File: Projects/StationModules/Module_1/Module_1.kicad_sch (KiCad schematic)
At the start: 55 parts, among them M1 BluePillStm32, U1 PC817, U2 L7805, U3 TC1047AxNB, U5 LM311, U6 6N137

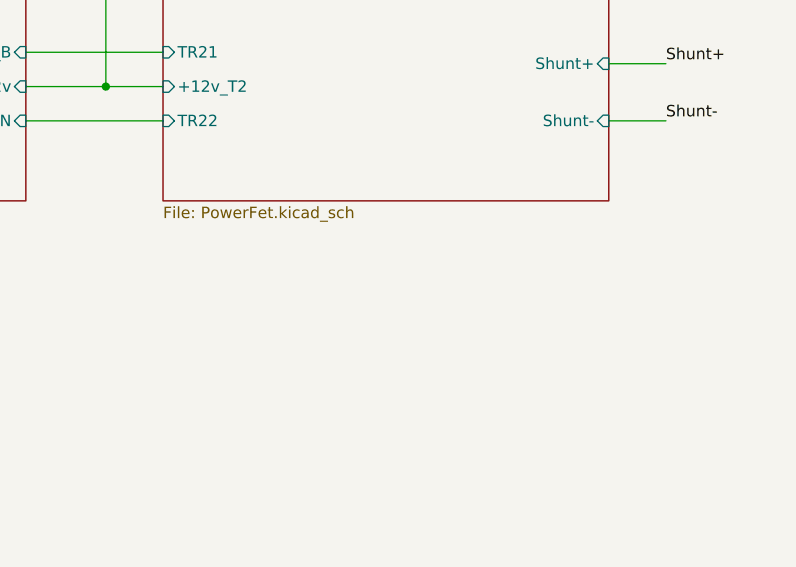
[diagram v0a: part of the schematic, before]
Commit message: Place elements 1
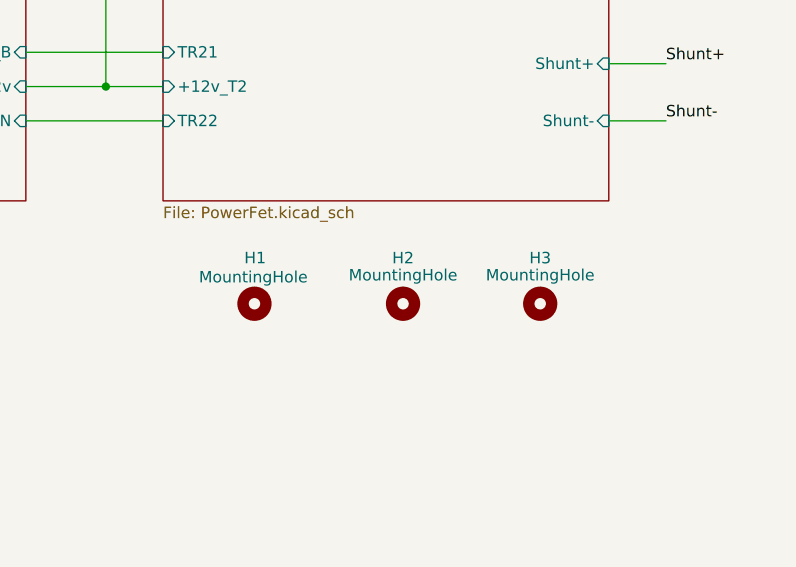
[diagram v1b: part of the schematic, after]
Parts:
- added H1, H2, H3: MountingHole, MountingHole:MountingHole_3.5mm, symbol Mechanical:MountingHole
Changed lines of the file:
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@@
+    )
+  )
+  (symbol (lib_id "Mechanical:MountingHole") (at 238.76 146.05 0) (unit 1)
+    (in_bom yes) (on_board yes) (dnp no)
+    (property "Reference" "H2" (at 238.76 140.97 0)
+      (effects (font (size 1.27 1.27)))
+    )
+    (property "Value" "MountingHole" (at 238.76 142.875 0)
+      (effects (font (size 1.27 1.27)))
+    )
+    (property "Footprint" "MountingHole:MountingHole_3.5mm" (at 238.76 146.05 0)
+      (effects (font (size 1.27 1.27)) hide)
+    )
+    (property "Datasheet" "~" (at 238.76 146.05 0)
+      (effects (font (size 1.27 1.27)) hide)
+    )
+    (instances
+      (project "Module_1"
+        (path "/52aeb9ce-9f3b-4d8f-8c36-7e23df4a5f32"
+          (reference "H2") (unit 1)
+        )
+      )
     )
   )
@@
     )
   )
+  (symbol (lib_id "Mechanical:MountingHole") (at 222.25 146.05 0) (unit 1)
+    (in_bom yes) (on_board yes) (dnp no)
+    (property "Reference" "H1" (at 221.1158 140.9618 0)
+      (effects (font (size 1.27 1.27)) (justify left))
+    )
+    (property "Value" "MountingHole" (at 216.0801 143.0922 0)
+      (effects (font (size 1.27 1.27)) (justify left))
+    )
+    (property "Footprint" "MountingHole:MountingHole_3.5mm" (at 222.25 146.05 0)
+      (effects (font (size 1.27 1.27)) hide)
+    )
+    (property "Datasheet" "~" (at 222.25 146.05 0)
+      (effects (font (size 1.27 1.27)) hide)
+    )
+    (instances
+      (project "Module_1"
+        (path "/52aeb9ce-9f3b-4d8f-8c36-7e23df4a5f32"
+          (reference "H1") (unit 1)
+        )
+      )
+    )
+  )
   (symbol (lib_id "Device:C_Small") (at 53.34 113.03 0) (unit 1)
     (in_bom yes) (on_board yes) (dnp no) (fields_autoplaced)
@@
         )
       )
+    )
+  )
+  (symbol (lib_id "Mechanical:MountingHole") (at 254 146.05 0) (unit 1)
+    (in_bom yes) (on_board yes) (dnp no)
+    (property "Reference" "H3" (at 254 140.97 0)
+      (effects (font (size 1.27 1.27)))
+    )
+    (property "Value" "MountingHole" (at 254 142.875 0)
+      (effects (font (size 1.27 1.27)))
+    )
+    (property "Footprint" "MountingHole:MountingHole_3.5mm" (at 254 146.05 0)
+      (effects (font (size 1.27 1.27)) hide)
+    )
+    (property "Datasheet" "~" (at 254 146.05 0)
+      (effects (font (size 1.27 1.27)) hide)
+    )
+    (instances
+      (project "Module_1"
+        (path "/52aeb9ce-9f3b-4d8f-8c36-7e23df4a5f32"
+          (reference "H3") (unit 1)
+        )
+      )

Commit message: Trace complit 1
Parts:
- added C29: 0,1uF, Capacitor_SMD:C_1206_3216Metric, symbol Device:C_Small
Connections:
- net +3.3V is gone; now on net +3V3: C1.1, M1.20 (3V3)
- net +5V: now also C29.1
- net GND: now also C29.2
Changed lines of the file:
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@@
   (junction (at 132.08 57.15) (diameter 0) (color 0 0 0 0)
   )
+  (junction (at 101.6 104.14) (diameter 0) (color 0 0 0 0)
+  )
   (junction (at 34.29 90.17) (diameter 0) (color 0 0 0 0)
   )
   (junction (at 59.69 137.16) (diameter 0) (color 0 0 0 0)
   )
+  (junction (at 22.86 80.01) (diameter 0) (color 0 0 0 0)
+  )
   (junction (at 52.07 137.16) (diameter 0) (color 0 0 0 0)
   )
@@
   )
   (junction (at 152.4 48.26) (diameter 0) (color 0 0 0 0)
-  )
-  (junction (at 22.86 80.01) (diameter 0) (color 0 0 0 0)
   )
   (junction (at 218.44 62.23) (diameter 0) (color 0 0 0 0)
@@
     (stroke (width 0) (type default))
   )
+  (wire (pts (xy 78.74 104.14) (xy 101.6 104.14))
+    (stroke (width 0) (type default))
+  )
   (wire (pts (xy 44.45 110.49) (xy 53.34 110.49))
     (stroke (width 0) (type default))
@@
     (stroke (width 0) (type default))
   )
+  (wire (pts (xy 78.74 110.49) (xy 78.74 120.65))
+    (stroke (width 0) (type default))
+  )
   (wire (pts (xy 152.4 22.86) (xy 152.4 25.4))
     (stroke (width 0) (type default))
@@
     (stroke (width 0) (type default))
   )
+  (wire (pts (xy 78.74 105.41) (xy 78.74 104.14))
+    (stroke (width 0) (type default))
+  )
   (wire (pts (xy 218.44 48.26) (xy 214.63 48.26))
     (stroke (width 0) (type default))
@@
   )
   (wire (pts (xy 101.6 78.74) (xy 105.41 78.74))
+    (stroke (width 0) (type default))
+  )
+  (wire (pts (xy 78.74 120.65) (xy 101.6 120.65))
     (stroke (width 0) (type default))
   )
@@
     )
   )
-  (symbol (lib_id "power:+3.3V") (at 22.86 80.01 0) (unit 1)
-    (in_bom yes) (on_board yes) (dnp no) (fields_autoplaced)
-    (property "Reference" "#PWR01" (at 22.86 83.82 0)
-      (effects (font (size 1.27 1.27)) hide)
-    )
-    (property "Value" "+3.3V" (at 22.86 76.2 0)
-      (effects (font (size 1.27 1.27)))
-    )
-    (property "Footprint" "" (at 22.86 80.01 0)
-      (effects (font (size 1.27 1.27)) hide)
-    )
-    (property "Datasheet" "" (at 22.86 80.01 0)
-      (effects (font (size 1.27 1.27)) hide)
-    )
-    (pin "1")
-    (instances
-      (project "Module_1"
-        (path "/52aeb9ce-9f3b-4d8f-8c36-7e23df4a5f32"
-          (reference "#PWR01") (unit 1)
-        )
-      )
-    )
-  )
   (symbol (lib_id "Z_led:Led") (at 118.11 71.12 0) (unit 1)
     (in_bom yes) (on_board yes) (dnp no)
@@
         (path "/52aeb9ce-9f3b-4d8f-8c36-7e23df4a5f32"
           (reference "R18") (unit 1)
+        )
+      )
+    )
+  )
+  (symbol (lib_id "Device:C_Small") (at 78.74 107.95 0) (unit 1)
+    (in_bom yes) (on_board yes) (dnp no) (fields_autoplaced)
+    (property "Reference" "C29" (at 81.28 107.3213 0)
+      (effects (font (size 1.27 1.27)) (justify left))
+    )
+    (property "Value" "0,1uF" (at 81.28 109.8613 0)
+      (effects (font (size 1.27 1.27)) (justify left))
+    )
+    (property "Footprint" "Capacitor_SMD:C_1206_3216Metric" (at 78.74 107.95 0)
+      (effects (font (size 1.27 1.27)) hide)
+    )
+    (property "Datasheet" "~" (at 78.74 107.95 0)
+      (effects (font (size 1.27 1.27)) hide)
+    )
+    (property "ID" "" (at 78.74 107.95 0)
+      (effects (font (size 1.27 1.27)) hide)
+    )
+    (pin "1")
+    (pin "2")
+    (instances
+      (project "Module_1"
+        (path "/52aeb9ce-9f3b-4d8f-8c36-7e23df4a5f32"
+          (reference "C29") (unit 1)
         )
       )
@@
         )
       )
+    )
+  )
+  (symbol (lib_id "power:+3V3") (at 22.86 80.01 0) (unit 1)
+    (in_bom yes) (on_board yes) (dnp no) (fields_autoplaced)
+    (property "Reference" "#PWR028" (at 22.86 83.82 0)
+      (effects (font (size 1.27 1.27)) hide)
+    )
+    (property "Value" "+3V3" (at 22.86 76.2 0)
+      (effects (font (size 1.27 1.27)))
+    )
+    (property "Footprint" "" (at 22.86 80.01 0)
+      (effects (font (size 1.27 1.27)) hide)
+    )
+    (property "Datasheet" "" (at 22.86 80.01 0)
+      (effects (font (size 1.27 1.27)) hide)
+    )
+    (pin "1")
+    (instances
+      (project "Module_1"
+        (path "/52aeb9ce-9f3b-4d8f-8c36-7e23df4a5f32"
+          (reference "#PWR028") (unit 1)
+        )
+      )

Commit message: Trace complit 2
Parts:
- U5: footprint Package_SO:SO-8_5.3x6.2mm_P1.27mm -> Package_SO:SO-8_3.9x4.9mm_P1.27mm
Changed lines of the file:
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@@
       (effects (font (size 1.27 1.27)))
     )
-    (property "Footprint" "Package_SO:SO-8_5.3x6.2mm_P1.27mm" (at 240.03 53.34 0)
+    (property "Footprint" "Package_SO:SO-8_3.9x4.9mm_P1.27mm" (at 240.03 53.34 0)
       (effects (font (size 1.27 1.27)) hide)
     )

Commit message: add bom module 1
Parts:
- added C30: 0,1uF, Capacitor_SMD:C_1206_3216Metric, symbol Device:C_Small
- C1, C11, C12, C16, C18, C2, C29, C5, C7, C8: LCSC (none) -> C82601; MFR.Part (none) -> CC1206KRX7R9BB104
- C10, C9: LCSC (none) -> C469628; MFR.Part (none) -> CC1206JRNPOBBN100
- C13, C14, C15: LCSC (none) -> C274377; MFR.Part (none) -> CC1206KRX7R9BB334
- C17: LCSC (none) -> C527247; MFR.Part (none) -> CC1206GRNPO9BN102
- C3, C6: LCSC (none) -> C88730; MFR.Part (none) -> 25PX470MEFC8X11.5
- C4: footprint Capacitor_Tantalum_SMD:CP_EIA-6032-28_Kemet-C -> Capacitor_Tantalum_SMD:CP_EIA-7343-15_Kemet-W; ID T495C107K016ATE200 -> (none); LCSC (none) -> C122302; MFR.Part (none) -> T491D107K020AT
- D1, D5, D6: LCSC (none) -> C2891733; MFR.Part (none) -> LL4148
- D2: LCSC (none) -> C3013853; MFR.Part (none) -> TLHR5400
- D3: LCSC (none) -> C5334366; MFR.Part (none) -> TLHY4405
- D4, D7: LCSC (none) -> C3001646; MFR.Part (none) -> TLHG4400
- J1: LCSC (none) -> C5665; MFR.Part (none) -> C5665
- JP1, JP2: LCSC (none) -> C6332196; MFR.Part (none) -> HB-PH3-25413PB2GOP
- R1, R11, R15, R9: LCSC (none) -> C136458; MFR.Part (none) -> RC1206JR-074K7L
- R10: LCSC (none) -> C137199; MFR.Part (none) -> RC1206JR-0715KL
- R12: LCSC (none) -> C137124; MFR.Part (none) -> RC1206JR-07680RL
- R13, R5, R6, R7: LCSC (none) -> C137152; MFR.Part (none) -> RC1206JR-07330RL
- R14, R18: LCSC (none) -> C137189; MFR.Part (none) -> RC1206JR-071K5L
- R16: LCSC (none) -> C246069; MFR.Part (none) -> RC1206JR-07360RL
- R17: LCSC (none) -> C112223; MFR.Part (none) -> RC1206JR-071KL
- R2: LCSC (none) -> C114948; MFR.Part (none) -> RC1206JR-07470RL
- R3, R4: value 4k7 -> 4,7k; LCSC (none) -> C136458; MFR.Part (none) -> RC1206JR-074K7L
- R8: LCSC (none) -> C113307; MFR.Part (none) -> RC1206JR-07100RL
- RV1, RV2: value 4k7 3296W -> 5k; LCSC (none) -> C118907; MFR.Part (none) -> 3296W-1-502
- U1: LCSC (none) -> C2833074; MFR.Part (none) -> PC817X2YSZW
- U2: LCSC (none) -> C2935188; MFR.Part (none) -> L7805ABP
- U3: LCSC (none) -> C50052; MFR.Part (none) -> TC1047AVNBTR
- U4: value ~ -> 78L05S; LCSC (none) -> C2858514; MFR.Part (none) -> 78L05S
- U5: LCSC (none) -> C2868397; MFR.Part (none) -> LM311PSR
- U6: LCSC (none) -> C142297; MFR.Part (none) -> 6N137
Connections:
- net GND: now also C30.2
- net OS: now also C30.1

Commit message: finaly on summer
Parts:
- D2: LCSC C3013853 -> C99771
- D3: LCSC C5334366 -> C85160
- D4, D7: LCSC C3001646 -> C2895476
- JP1, JP2: LCSC C6332196 -> C49257
- R17: LCSC C112223 -> C4410; MFR.Part RC1206JR-071KL -> 1206W4F1001T5E
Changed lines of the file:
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@@
       (effects (font (size 1.27 1.27)) hide)
     )
-    (property "LCSC" "C3013853" (at 118.11 64.77 0)
+    (property "LCSC" "C99771" (at 118.11 64.77 0)
       (effects (font (size 1.27 1.27)) hide)
     )
@@
       (effects (font (size 1.27 1.27)) hide)
     )
-    (property "LCSC" "C3001646" (at 179.07 48.26 0)
+    (property "LCSC" "C2895476" (at 179.07 48.26 0)
       (effects (font (size 1.27 1.27)) hide)
     )
@@
       (effects (font (size 1.27 1.27)) hide)
     )
-    (property "LCSC" "C6332196" (at 130.81 181.61 0)
+    (property "LCSC" "C49257" (at 130.81 181.61 0)
       (effects (font (size 1.27 1.27)) hide)
     )
@@
       (effects (font (size 1.27 1.27)) hide)
     )
-    (property "LCSC" "C5334366" (at 118.11 71.12 0)
+    (property "LCSC" "C85160" (at 118.11 71.12 0)
       (effects (font (size 1.27 1.27)) hide)
     )
@@
       (effects (font (size 1.27 1.27)) hide)
     )
-    (property "MFR.Part" "RC1206JR-071KL" (at 227.33 27.94 0)
-      (effects (font (size 1.27 1.27)) hide)
-    )
-    (property "Description" "250mW Thick Film Resistors ±100ppm/℃ ±5% 1kΩ 1206 Chip Resistor - Surface Mount ROHS" (at 227.33 27.94 0)
-      (effects (font (size 1.27 1.27)) hide)
-    )
-    (property "LCSC" "C112223" (at 227.33 27.94 0)
+    (property "MFR.Part" "1206W4F1001T5E" (at 227.33 27.94 0)
+      (effects (font (size 1.27 1.27)) hide)
+    )
+    (property "Description" "250mW Thick Film Resistors ±1% 1kΩ 1206 Chip Resistor - Surface Mount ROHS" (at 227.33 27.94 0)
+      (effects (font (size 1.27 1.27)) hide)
+    )
+    (property "LCSC" "C4410" (at 227.33 27.94 0)
       (effects (font (size 1.27 1.27)) hide)
     )
@@
       (effects (font (size 1.27 1.27)) hide)
     )
-    (property "LCSC" "C6332196" (at 130.81 165.1 0)
+    (property "LCSC" "C49257" (at 130.81 165.1 0)
       (effects (font (size 1.27 1.27)) hide)
     )
@@
       (effects (font (size 1.27 1.27)) hide)
     )
-    (property "LCSC" "C3001646" (at 118.11 78.74 0)
-      (effects (font (size 1.27 1.27)) hide)
-    )
+    (property "LCSC" "C2895476" (at 118.11 78.74 0)
+      (effects (font (size 1.27 1.27)) hide)
+    )

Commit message: change module1,2
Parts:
- C10, C9: value 10pF -> 10nF; LCSC C469628 -> C9194; MFR.Part CC1206JRNPOBBN100 -> 1206B103K102NT
- R16: value 360 -> 150; LCSC C246069 -> C25353; MFR.Part RC1206JR-07360RL -> 1206W4J0151T5E
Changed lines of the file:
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@@
       (effects (font (size 1.27 1.27)) (justify right))
     )
-    (property "Value" "360" (at 220.98 57.785 0)
+    (property "Value" "150" (at 220.98 57.785 0)
       (effects (font (size 1.27 1.27)) (justify right))
     )
@@
       (effects (font (size 1.27 1.27)) hide)
     )
-    (property "MFR.Part" "RC1206JR-07360RL" (at 218.44 55.88 0)
-      (effects (font (size 1.27 1.27)) hide)
-    )
-    (property "Description" "250mW Thick Film Resistors ±100ppm/℃ ±5% 360Ω 1206 Chip Resistor - Surface Mount ROHS" (at 218.44 55.88 0)
-      (effects (font (size 1.27 1.27)) hide)
-    )
-    (property "LCSC" "C246069" (at 218.44 55.88 0)
+    (property "MFR.Part" "1206W4J0151T5E" (at 218.44 55.88 0)
+      (effects (font (size 1.27 1.27)) hide)
+    )
+    (property "Description" "250mW Thick Film Resistors ±100ppm/℃ ±5% 150Ω 1206 Chip Resistor - Surface Mount ROHS" (at 218.44 55.88 0)
+      (effects (font (size 1.27 1.27)) hide)
+    )
+    (property "LCSC" "C25353" (at 218.44 55.88 0)
       (effects (font (size 1.27 1.27)) hide)
     )
@@
       (effects (font (size 1.27 1.27)) (justify left))
     )
-    (property "Value" "10pF" (at 123.19 142.8813 0)
+    (property "Value" "10nF" (at 123.19 142.8813 0)
       (effects (font (size 1.27 1.27)) (justify left))
     )
@@
       (effects (font (size 1.27 1.27)) hide)
     )
-    (property "MFR.Part" "CC1206JRNPOBBN100" (at 120.65 140.97 0)
-      (effects (font (size 1.27 1.27)) hide)
-    )
-    (property "Description" "500V 10pF NP0 ±5% 1206 Multilayer Ceramic Capacitors MLCC - SMD/SMT ROHS" (at 120.65 140.97 0)
-      (effects (font (size 1.27 1.27)) hide)
-    )
-    (property "LCSC" "C469628" (at 120.65 140.97 0)
+    (property "MFR.Part" "1206B103K102NT" (at 120.65 140.97 0)
+      (effects (font (size 1.27 1.27)) hide)
+    )
+    (property "Description" "1kV 10nF X7R ±10% 1206 Multilayer Ceramic Capacitors MLCC - SMD/SMT ROHS" (at 120.65 140.97 0)
+      (effects (font (size 1.27 1.27)) hide)
+    )
+    (property "LCSC" "C9194" (at 120.65 140.97 0)
       (effects (font (size 1.27 1.27)) hide)
     )
@@
       (effects (font (size 1.27 1.27)) (justify left))
     )
-    (property "Value" "10pF" (at 114.3 178.4413 0)
+    (property "Value" "10nF" (at 114.3 178.4413 0)
       (effects (font (size 1.27 1.27)) (justify left))
     )
@@
       (effects (font (size 1.27 1.27)) hide)
     )
-    (property "MFR.Part" "CC1206JRNPOBBN100" (at 111.76 176.53 0)
-      (effects (font (size 1.27 1.27)) hide)
-    )
-    (property "Description" "500V 10pF NP0 ±5% 1206 Multilayer Ceramic Capacitors MLCC - SMD/SMT ROHS" (at 111.76 176.53 0)
-      (effects (font (size 1.27 1.27)) hide)
-    )
-    (property "LCSC" "C469628" (at 111.76 176.53 0)
-      (effects (font (size 1.27 1.27)) hide)
-    )
+    (property "MFR.Part" "1206B103K102NT" (at 111.76 176.53 0)
+      (effects (font (size 1.27 1.27)) hide)
+    )
+    (property "Description" "1kV 10nF X7R ±10% 1206 Multilayer Ceramic Capacitors MLCC - SMD/SMT ROHS" (at 111.76 176.53 0)
+      (effects (font (size 1.27 1.27)) hide)
+    )
+    (property "LCSC" "C9194" (at 111.76 176.53 0)
+      (effects (font (size 1.27 1.27)) hide)
+    )

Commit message: change on 25_02_24
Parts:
- C1, C10, C11, C12, C13, C14, C15, C16, C17, C18, C2, C29, C3, C30, C4, C5, C6, C7, C8, C9, D1, D2, D3, D4, D5, D6, D7, J1, JP1, JP2, R1, R10, R11, R13, R14, R15, R16, R17, R18, R3, R4, R5, R6, R7, R8, R9, RV1, RV2, U1, U3, U4, U5, U6: Mounting (none) -> Yes
- H1, H2, H3, M1: Mounting (none) -> No
- R12: LCSC C137124 -> C25392; MFR.Part RC1206JR-07680RL -> 1206W4J0681T5E; Mounting (none) -> Yes
- R2: LCSC C114948 -> C114945; MFR.Part RC1206JR-07470RL -> RC1206FR-07470RL; Mounting (none) -> Yes
- U2: LCSC C2935188 -> C3795; MFR.Part L7805ABP -> L7805CV-DG; Mounting (none) -> Yes
